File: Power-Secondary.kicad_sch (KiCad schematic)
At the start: 34 parts, among them J1 SUPP PWR MON, J2 SUPP PWR 1, J3 SUPP PWR 2, J4 DCDC SUPPLY, J5 FUSE +12V, Q1 S1G1D2S2G2D1, Q1A1 SUP90P06, Q1A2 SUP90P06, Q1A3 SUP90P06, Q1A4 SUP90P06, Q2 S1G1D2S2G2D1, Q3 S1G1D2S2G2D1

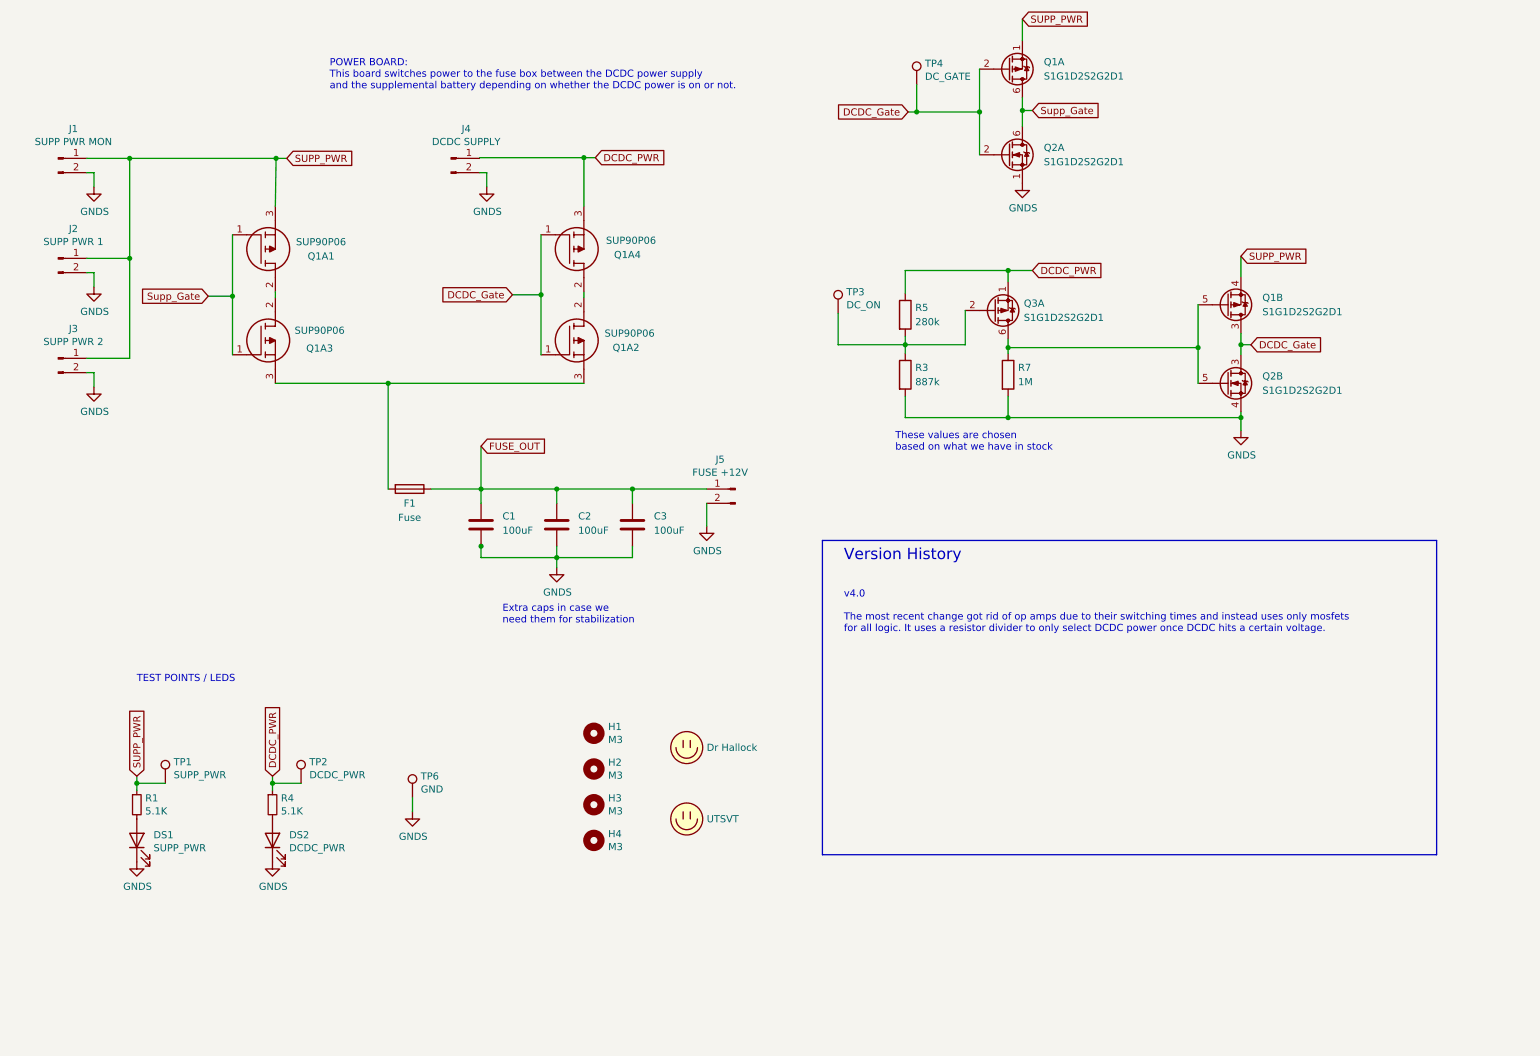
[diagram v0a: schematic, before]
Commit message: Fixed DRC and ERC errors in Kicad 7
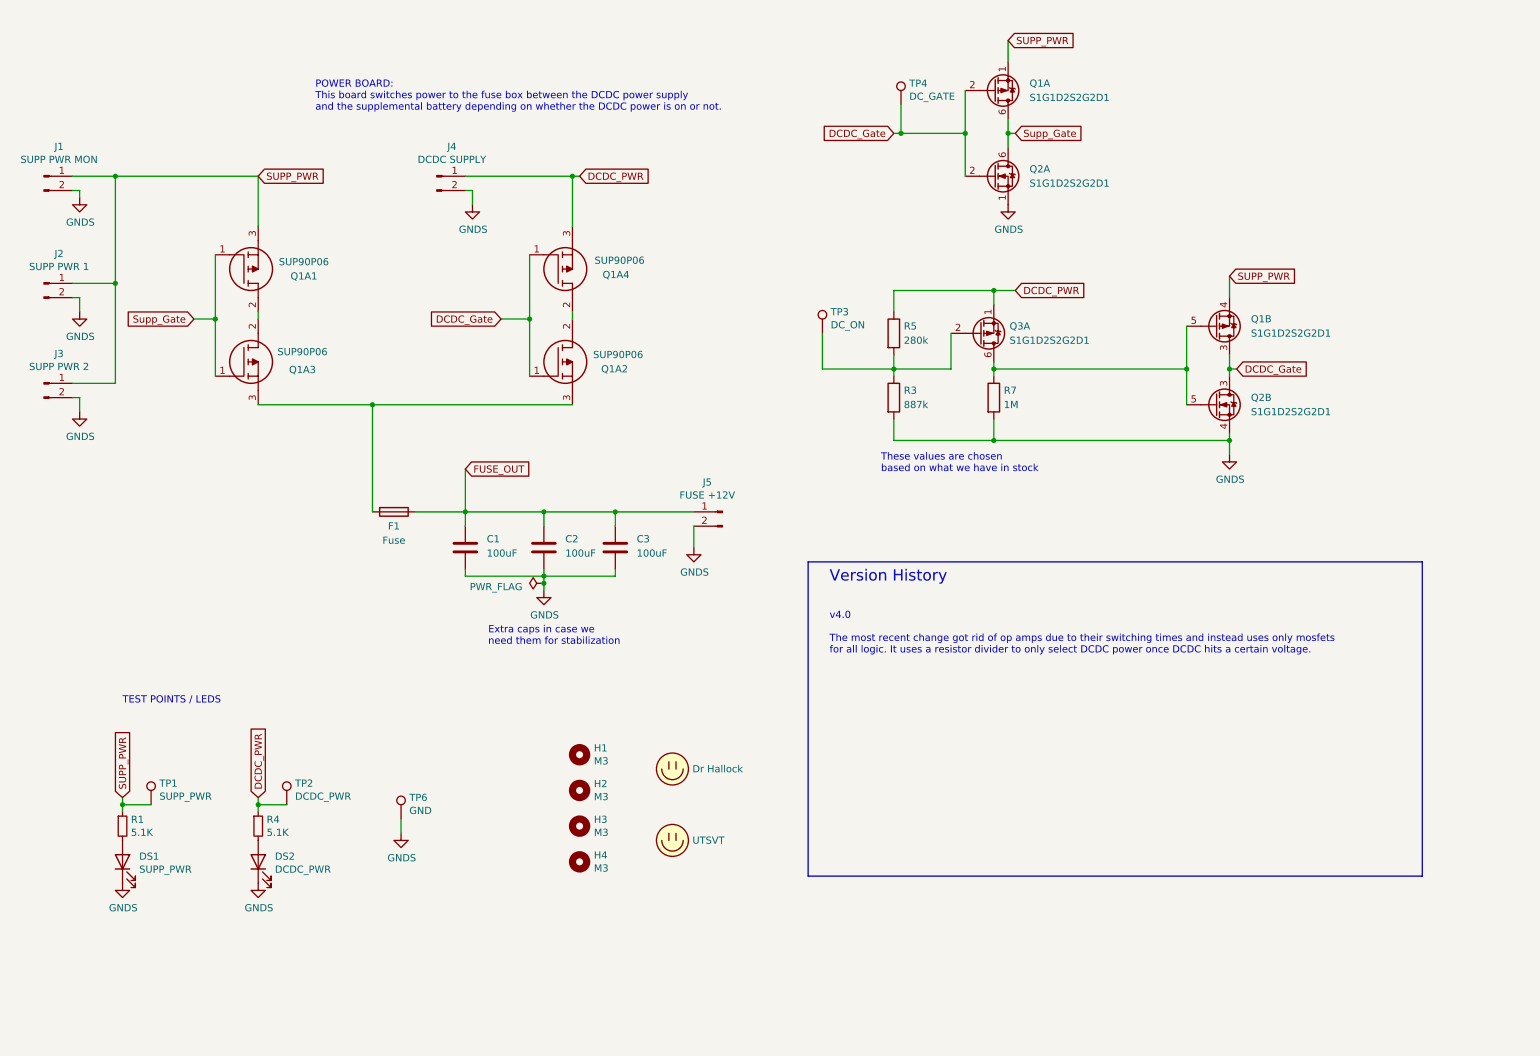
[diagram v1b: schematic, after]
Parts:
- J1, J2, J3, J4, J5: symbol Connector:Conn_01x02_Male -> Connector:Conn_01x02_Pin
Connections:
- net DCDC_PWR: now also J4.1 (Pin_1)
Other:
- moved on the sheet: C1, C2, C3, DS1, DS2, F1, H1, H2, H3, H4, J1, J2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

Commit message: Updated datasheets
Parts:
- Q1A1, Q1A2, Q1A3, Q1A4: Manufacturer_Name Infineon -> (none); Manufacturer_Part_Number AUIRF4905 -> (none); Mouser Part Number 942-AUIRF4905 -> (none); Mouser Price/Stock https://www.mouser.co.uk/ProductDetail/Infineon-Technologie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 -> (none)
- R3: value 887k -> 820k

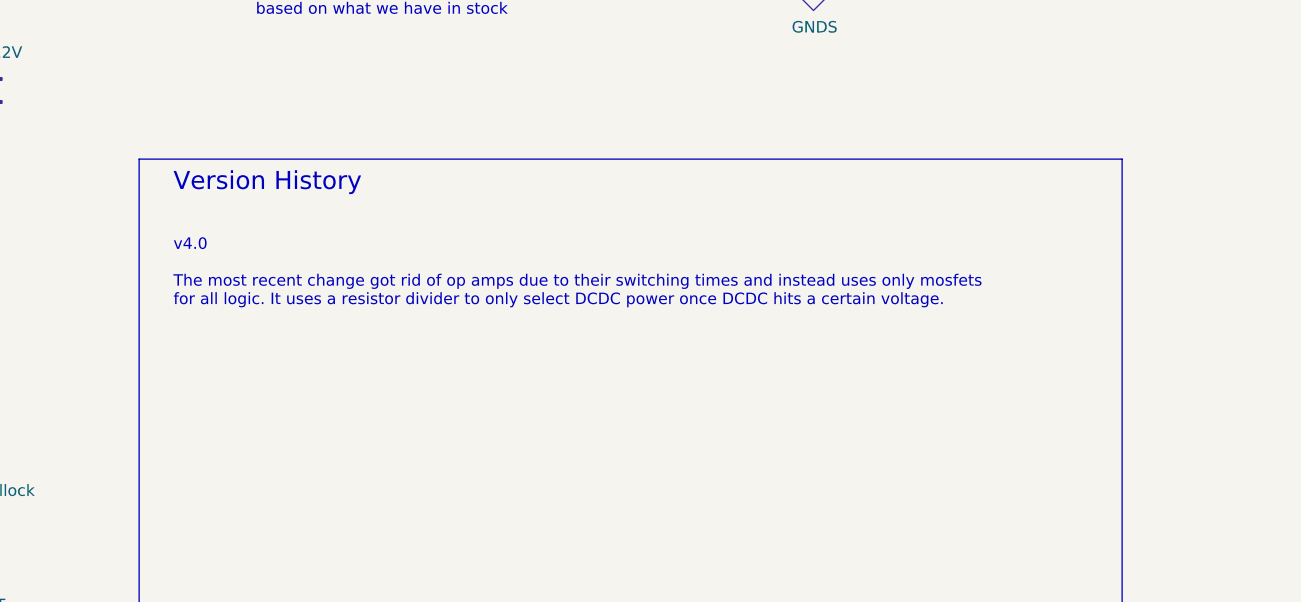
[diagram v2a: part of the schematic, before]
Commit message: Updated 3D models
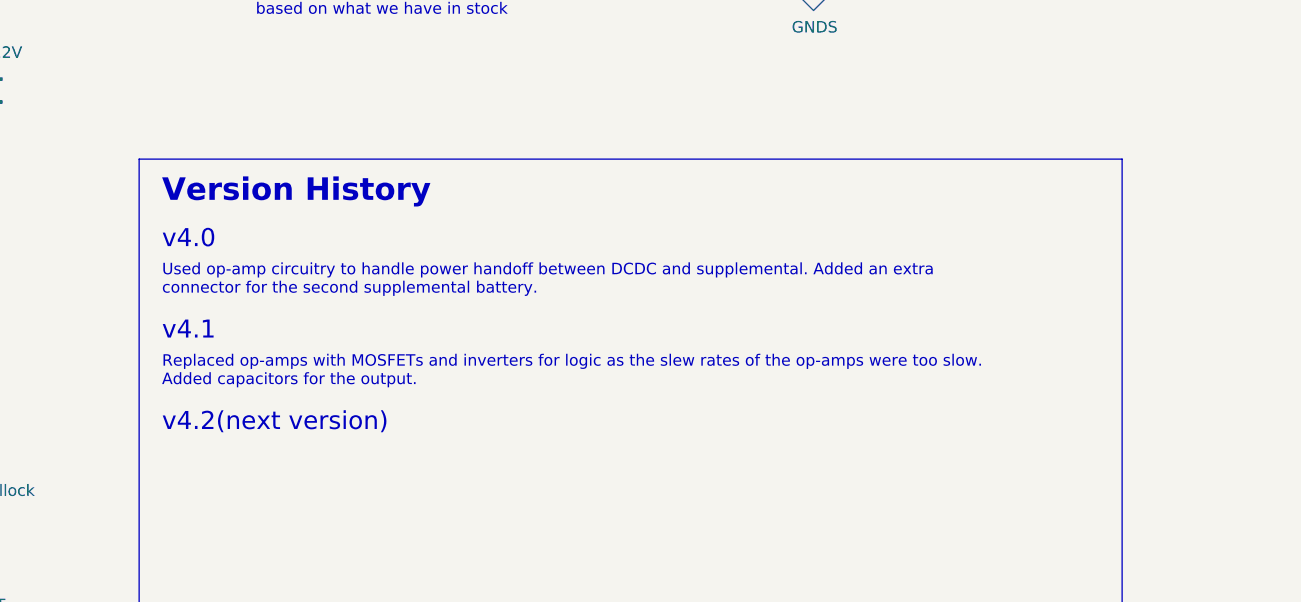
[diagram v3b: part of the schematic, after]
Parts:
- Q1A1, Q1A2, Q1A3, Q1A4: footprint UTSVT_PowerSupp:TO254P465X1031X1954-3P -> UTSVT_PowerSupp:SUP90P06-PCHAN-ENH-PWR-MOSFET
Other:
- note added: "Replaced op-amps with MOSFETs and inverters for logic as the slew rates of the op-amps were too slow. Added capacitors for the output."
- note added: "Used op-amp circuitry to handle power handoff between DCDC and supplemental. Added an extra connector for the second supplemental battery."
- note added: "v4.0"
- note added: "v4.1"
- note added: "v4.2(next version)"
- note removed: "v4.0 The most recent change got rid of op amps due to their switching times and instead uses only mosfets for all logic. It uses a resistor divider to only select DCDC power once DCDC hits a certain voltage."
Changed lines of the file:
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@@
     (fill (type none))
   )
-  (text "v4.0\n\nThe most recent change got rid of op amps due to their switching times and instead uses only mosfets\nfor all logic. It uses a resistor divider to only select DCDC power once DCDC hits a certain voltage."
-    (at 157.48 127 0)
+  (text "Used op-amp circuitry to handle power handoff between DCDC and supplemental. Added an extra \nconnector for the second supplemental battery."
+    (at 156.21 125.73 0)
     (effects (font (size 1.27 1.27)) (justify left bottom))
   )
@@
     (effects (font (size 1.27 1.27)) (justify left bottom))
   )
+  (text "v4.1" (at 156.21 130.81 0)
+    (effects (font (face "Calibri") (size 2 2)) (justify left bottom))
+  )
   (text "POWER BOARD:\nThis board switches power to the fuse box between the DCDC power supply\nand the supplemental battery depending on whether the DCDC power is on or not."
     (at 66.04 30.48 0)
     (effects (font (size 1.27 1.27)) (justify left bottom))
   )
-  (text "Version History" (at 157.48 114.3 0)
-    (effects (font (size 2 2)) (justify left bottom))
+  (text "Version History" (at 156.21 115.57 0)
+    (effects (font (face "Calibri") (size 2.5 2.5) (thickness 0.5) bold) (justify left bottom))
   )
   (text "Extra caps in case we\nneed them for stabilization\n\n"
@@
     (effects (font (size 1.27 1.27)) (justify left bottom))
   )
+  (text "v4.2(next version)" (at 156.21 140.97 0)
+    (effects (font (face "Calibri") (size 2 2)) (justify left bottom))
+  )
+  (text "v4.0" (at 156.21 120.65 0)
+    (effects (font (face "Calibri") (size 2 2)) (justify left bottom))
+  )
   (text "TEST POINTS / LEDS" (at 31.75 135.89 0)
+    (effects (font (size 1.27 1.27)) (justify left bottom))
+  )
+  (text "Replaced op-amps with MOSFETs and inverters for logic as the slew rates of the op-amps were too slow.\nAdded capacitors for the output.\n"
+    (at 156.21 135.89 0)
     (effects (font (size 1.27 1.27)) (justify left bottom))
   )
@@
       (effects (font (size 1.27 1.27)))
     )
-    (property "Footprint" "UTSVT_PowerSupp:TO254P465X1031X1954-3P" (at 115.57 54.61 0)
+    (property "Footprint" "UTSVT_PowerSupp:SUP90P06-PCHAN-ENH-PWR-MOSFET" (at 115.57 54.61 0)
       (effects (font (size 1.27 1.27)) (justify left) hide)
     )
@@
       (effects (font (size 1.27 1.27)))
     )
-    (property "Footprint" "UTSVT_PowerSupp:TO254P465X1031X1954-3P" (at 115.57 78.74 0)
+    (property "Footprint" "UTSVT_PowerSupp:SUP90P06-PCHAN-ENH-PWR-MOSFET" (at 115.57 78.74 0)
       (effects (font (size 1.27 1.27)) (justify left) hide)
     )
@@
       (effects (font (size 1.27 1.27)))
     )
-    (property "Footprint" "UTSVT_PowerSupp:TO254P465X1031X1954-3P" (at 59.69 78.74 0)
+    (property "Footprint" "UTSVT_PowerSupp:SUP90P06-PCHAN-ENH-PWR-MOSFET" (at 59.69 78.74 0)
       (effects (font (size 1.27 1.27)) (justify left) hide)
     )
@@
       (effects (font (size 1.27 1.27)))
     )
-    (property "Footprint" "UTSVT_PowerSupp:TO254P465X1031X1954-3P" (at 59.69 54.61 0)
-      (effects (font (size 1.27 1.27)) (justify left) hide)
-    )
+    (property "Footprint" "UTSVT_PowerSupp:SUP90P06-PCHAN-ENH-PWR-MOSFET" (at 59.69 54.61 0)
+      (effects (font (size 1.27 1.27)) (justify left) hide)
+    )

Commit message: Updated README and version history
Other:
- note added: "Need to be able to handle a range of inputs from the supplemental battery. Need to stabilize output voltage at 12 volts. It is difficult to know at exactly what voltage DCDC will get selected due to the range of threshold voltages for Q3(switching could be somewhere from 5 to 11.95 volts)."
- note added: "Power Board"
- note added: "This board switches power to the fuse box between the DCDC power supply and the supplemental battery depending on whether the DCDC power is on or not."
- note removed: "POWER BOARD: This board switches power to the fuse box between the DCDC power supply and the supplemental battery depending on whether the DCDC power is on or not."
- moved on the sheet: C1, C2, C3, F1, J1, J2, J3, J4, J5, Q1A1, Q1A2, Q1A3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

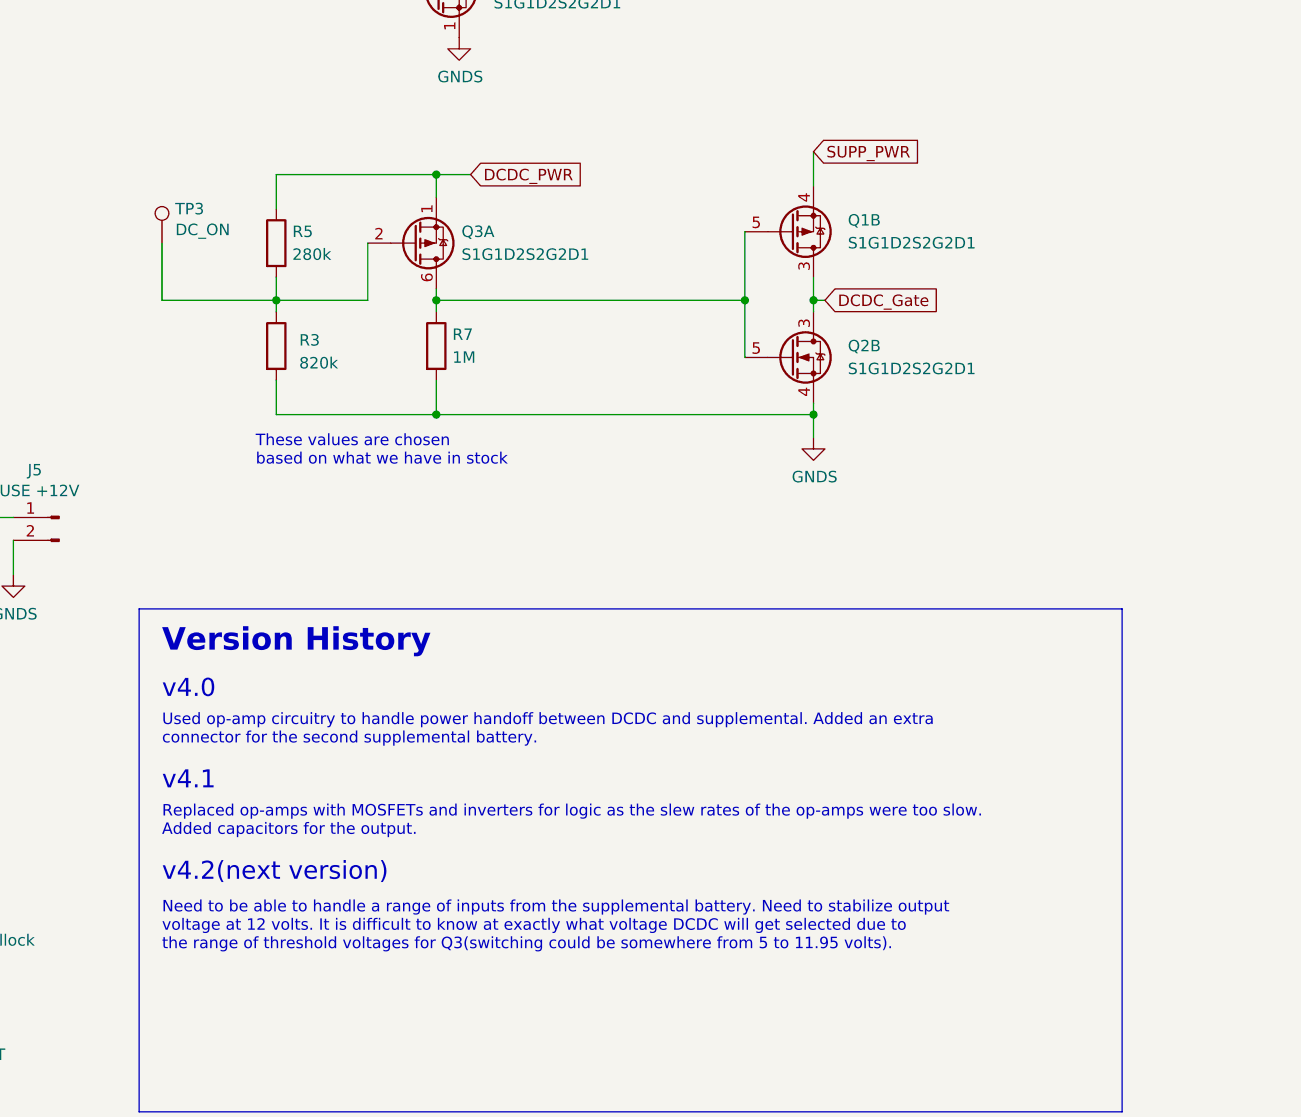
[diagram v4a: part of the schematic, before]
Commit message: Replaced resistor divider with zener
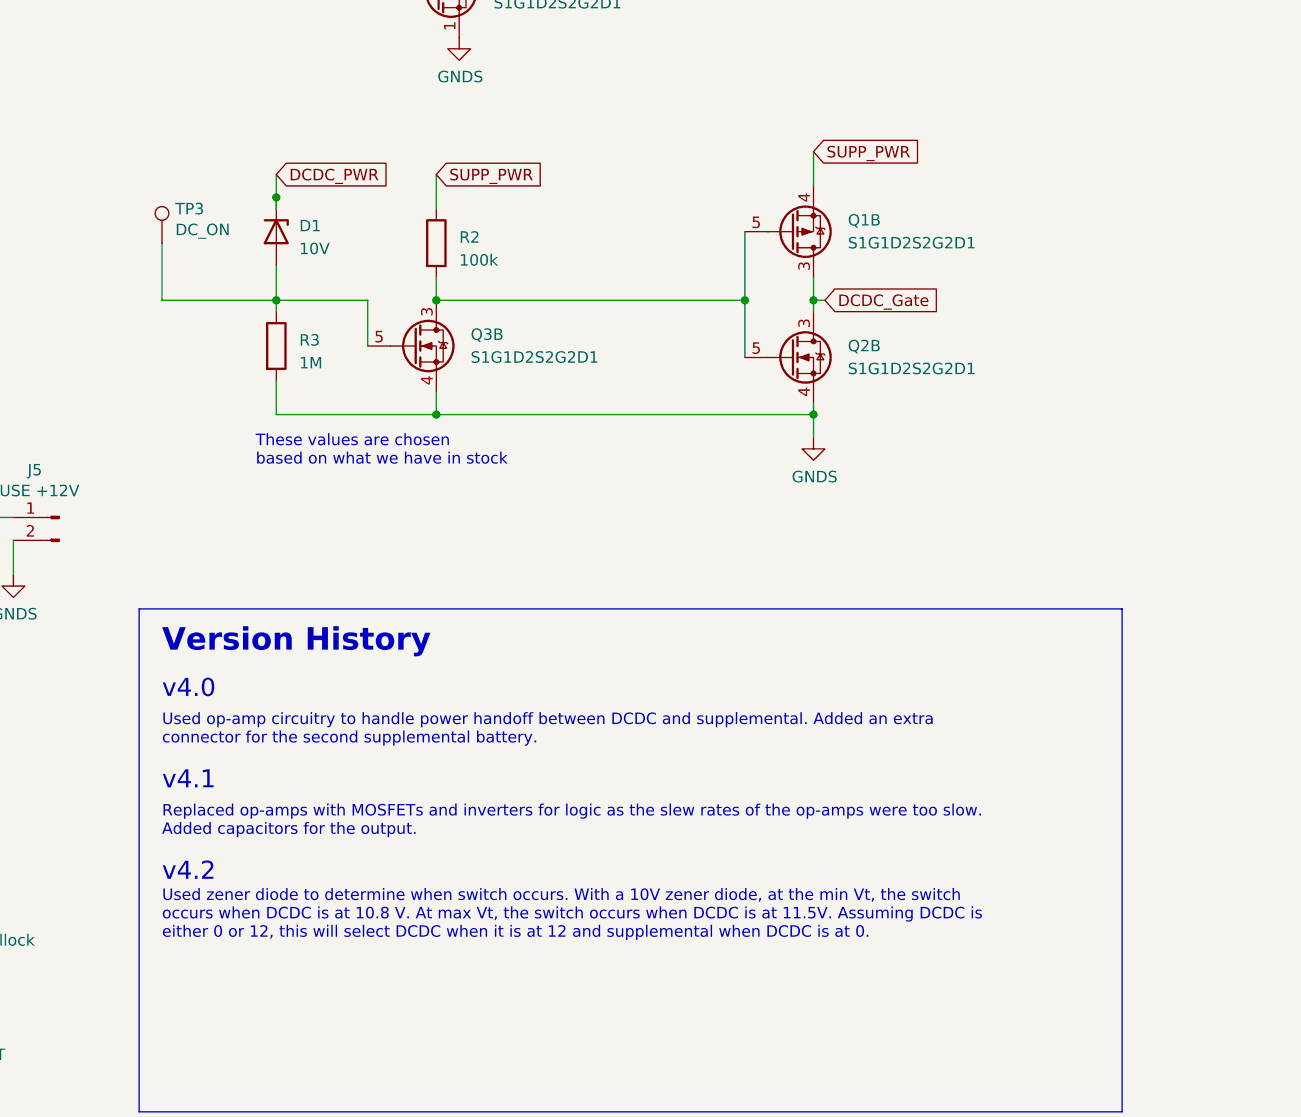
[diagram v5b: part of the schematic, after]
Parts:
- removed Q3: S1G1D2S2G2D1, UTSVT_PowerSupp:SOT65P210X100-6N, symbol Device:Q_Dual_PMOS_S1G1D2S2G2D1
- removed R5: 280k, Resistor_SMD:R_0603_1608Metric, symbol Device:R
- removed R7: 1M, Resistor_SMD:R_0603_1608Metric, symbol Device:R
- added D1: 10V, UTSVT_PowerSupp:SOD2512X110N, symbol Device:D_Zener
- added Q3: S1G1D2S2G2D1, UTSVT_PowerSupp:SOT65P210X100-6N, symbol Device:Q_Dual_NMOS_S1G1D2S2G2D1
- added R2: 100k, Resistor_SMD:R_0603_1608Metric, symbol Device:R
- R3: value 820k -> 1M
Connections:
- net DCDC_PWR: now also D1.1 (K)
- net GNDS: now also Q3.4 (S)
- net SUPP_PWR: now also R2.1
- net at R3.1, TP3.1: now also D1.2 (A), Q3.5 (G)
- net at Q1.5 (G), Q2.5 (G): now also Q3.3 (D), R2.2
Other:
- note added: "Used zener diode to determine when switch occurs. With a 10V zener diode, at the min Vt, the switch occurs when DCDC is at 10.8 V. At max Vt, the switch occurs when DCDC is at 11.5V. Assuming DCDC is either 0 or 12, this will select DCDC when it is at 12 and supplemental when DCDC is at 0."
- note added: "v4.2"
- note removed: "Need to be able to handle a range of inputs from the supplemental battery. Need to stabilize output voltage at 12 volts. It is difficult to know at exactly what voltage DCDC will get selected due to the range of threshold voltages for Q3(switching could be somewhere from 5 to 11.95 volts)."
- note removed: "v4.2(next version)"
